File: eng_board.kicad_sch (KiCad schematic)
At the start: 54 parts, among them J1 Conn_01x12, J2 Conn_01x12, U1 LT3420, U12 TLV74318, U19 XS-LCC-01, U2 ADS7047, U5 ADS7047, U6 ADS7047, U7 TLV74325

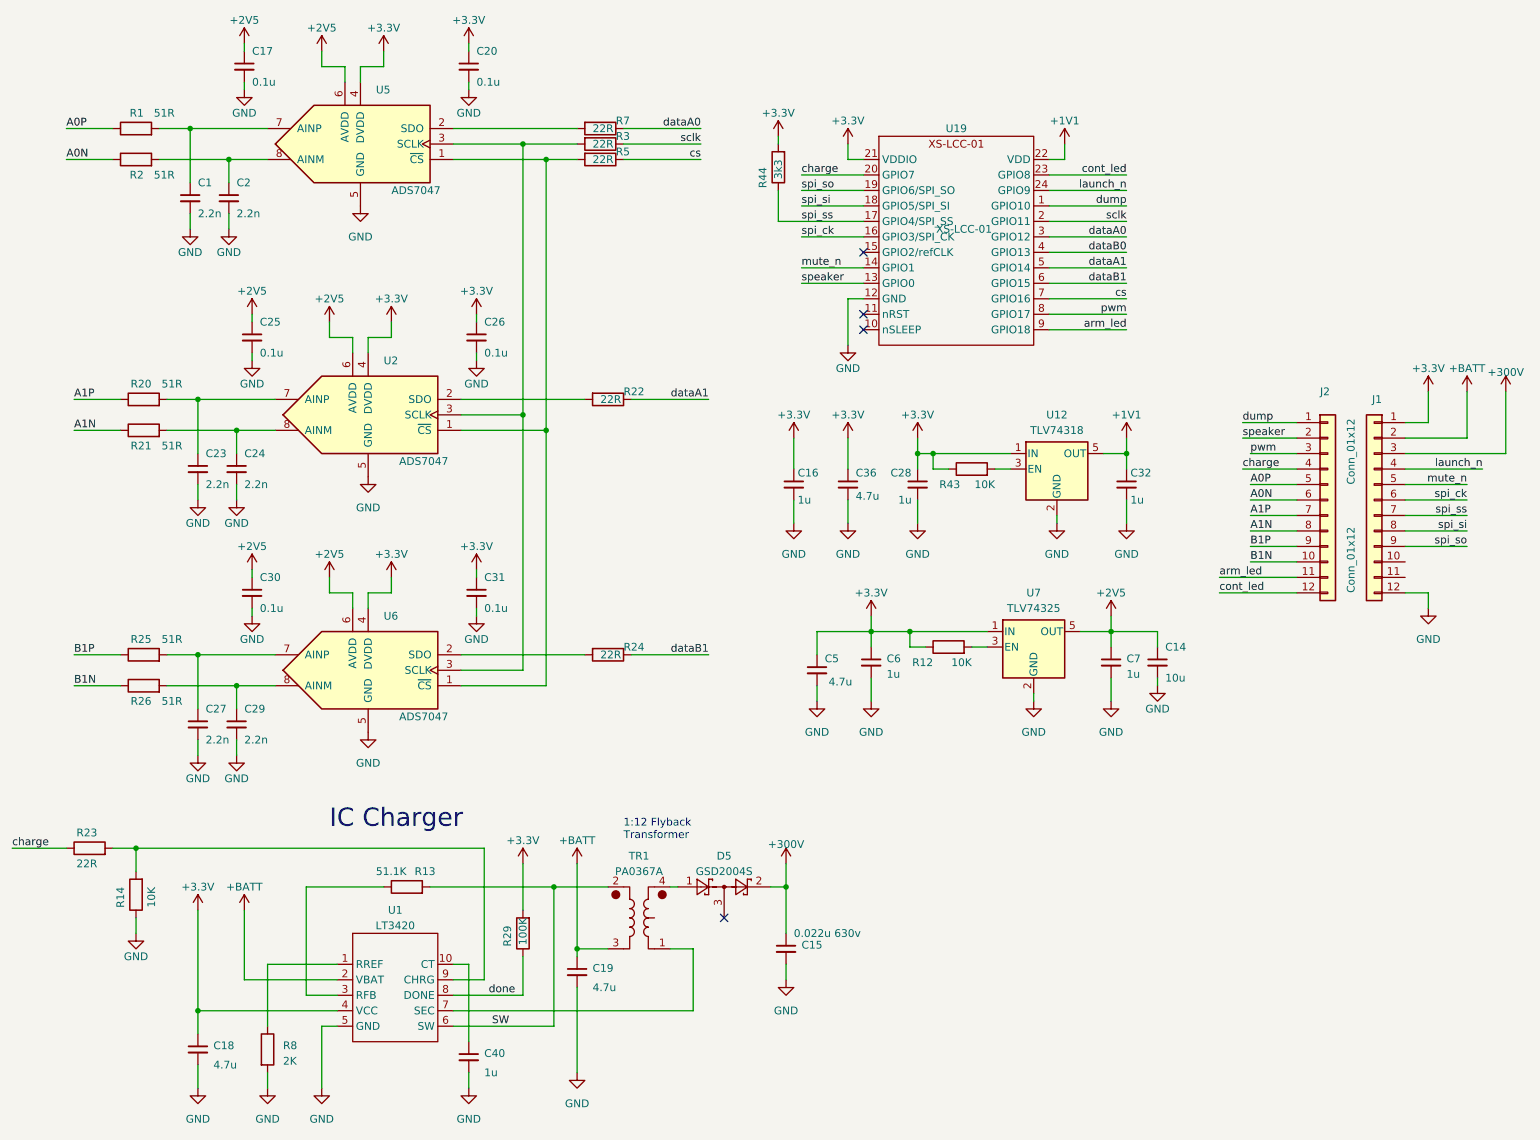
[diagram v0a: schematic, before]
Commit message: change back to dual ADCs (with internal refs) for now. Leave the low cost ADCs to the future
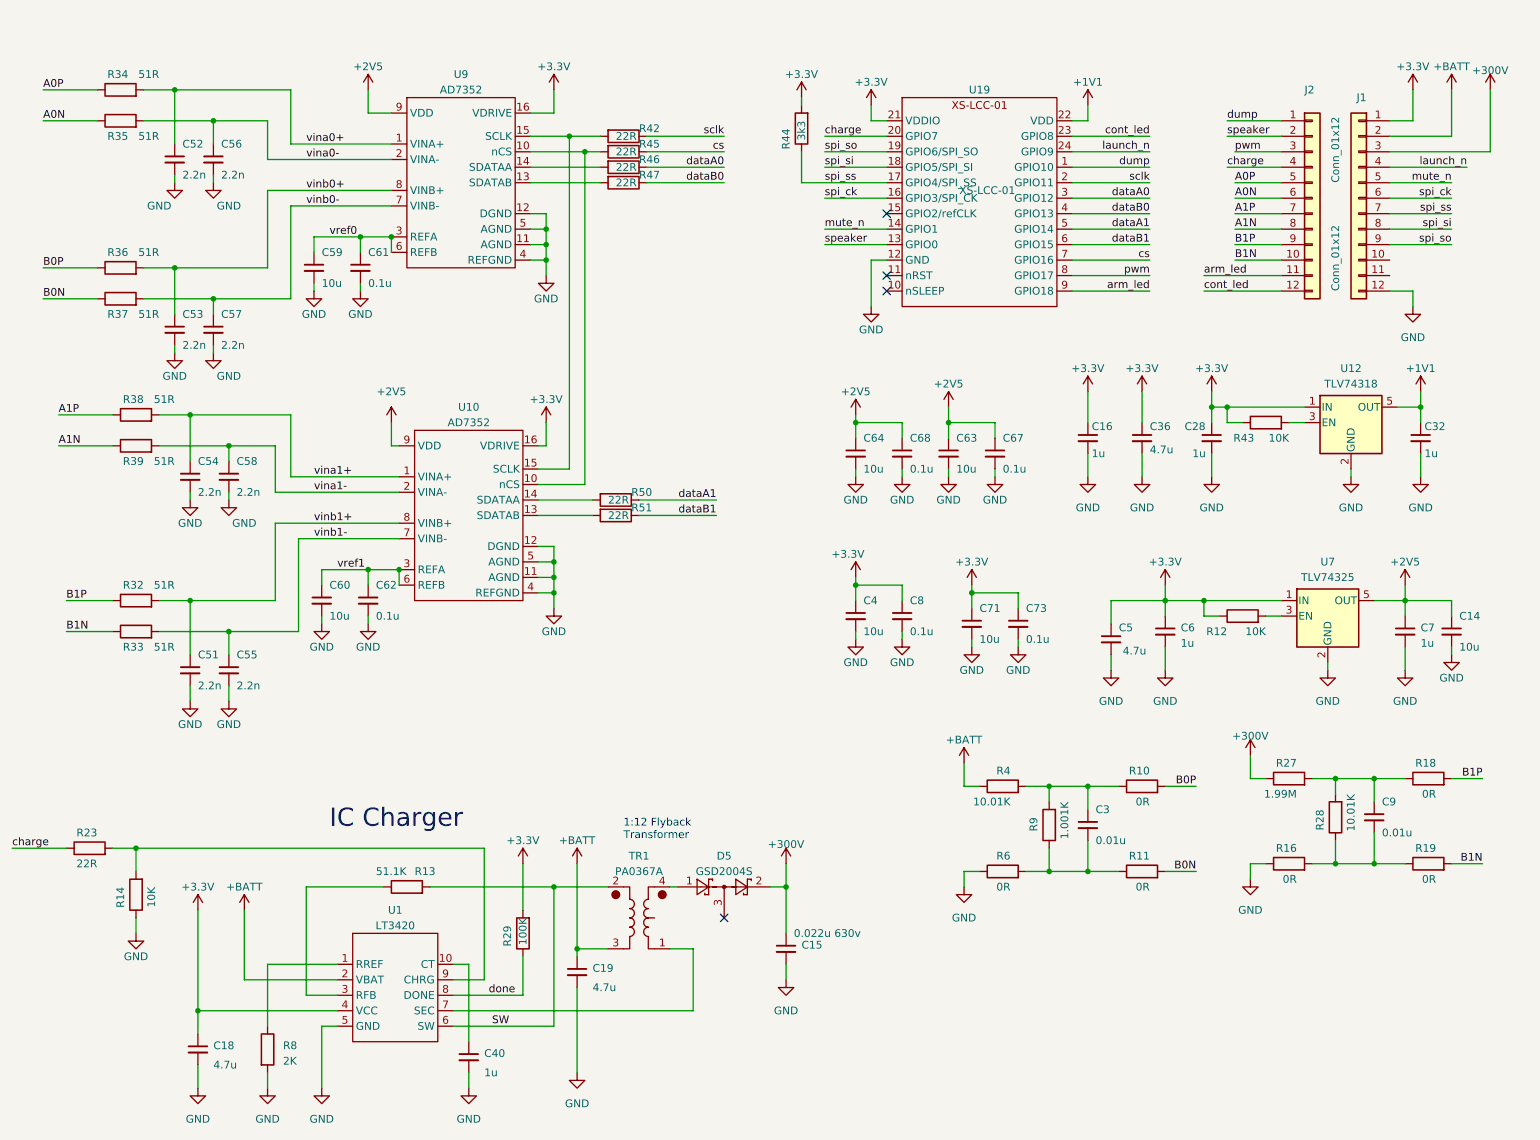
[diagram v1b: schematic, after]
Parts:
- removed C1, C2, C23, C24, C27, C29: 2.2n, Capacitor_SMD:C_0603_1608Metric, symbol Device:C_Small
- removed C17, C20, C25, C26, C30, C31: 0.1u, Capacitor_SMD:C_0603_1608Metric, symbol Device:C_Small
- removed R1, R2, R20, R21, R25, R26: 51R, Resistor_SMD:R_0603_1608Metric, symbol Device:R
- removed R22, R24, R3, R5, R7: 22R, Resistor_SMD:R_0603_1608Metric, symbol Device:R
- removed U2, U5, U6: ADS7047, Package_DFN_QFN:VDFN-8-1EP_2x2mm_P0.5mm_EP0.9x1.7mm, symbol myspace:ADS7047
- added C3, C9: 0.01u, Capacitor_SMD:C_0603_1608Metric, symbol Device:C_Small
- added C4, C59, C60, C63, C64, C71: 10u, Capacitor_SMD:C_1206_3216Metric, symbol Device:C_Small
- added C51, C52, C53, C54, C55, C56, C57, C58: 2.2n, Capacitor_SMD:C_0603_1608Metric, symbol Device:C_Small
- added C61, C62, C67, C68, C73, C8: 0.1u, Capacitor_SMD:C_0603_1608Metric, symbol Device:C_Small
- added R10, R11, R16, R18, R19, R6: 0R, Resistor_SMD:R_0603_1608Metric, symbol Device:R
- added R27: 1.99M, Resistor_SMD:R_0603_1608Metric, symbol Device:R
- added R28, R4: 10.01K, Resistor_SMD:R_0603_1608Metric, symbol Device:R
- added R32, R33, R34, R35, R36, R37, R38, R39: 51R, Resistor_SMD:R_0603_1608Metric, symbol Device:R
- added R42, R45, R46, R47, R50, R51: 22R, Resistor_SMD:R_0603_1608Metric, symbol Device:R
- added R9: 1.001K, Resistor_SMD:R_0603_1608Metric, symbol Device:R
- added U10, U9: AD7352, Package_SO:TSSOP-16_4.4x5mm_P0.65mm, symbol myspace:AD7352
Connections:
- net +2V5: now also C63.1, C64.1, C67.1, C68.1, U10.9 (VDD), U9.9 (VDD)
- net +3.3V: now also C4.1, C71.1, C73.1, C8.1, U10.16 (VDRIVE), U9.16 (VDRIVE)
- net +300V: now also R27.1
- net +BATT: now also R4.1
- net A0N: now also R35.1
- net A0P: now also R34.1
- net A1N: now also R39.1
- net A1P: now also R38.1
- net B1N: now also R19.2, R33.1
- net B1P: now also R18.2, R32.1
- net GND: now also C4.2, C51.2, C52.2, C53.2, C54.2, C55.2, C56.2, C57.2, C58.2, C59.2, C60.2, C61.2, C62.2, C63.2, C64.2, C67.2, C68.2, C71.2, C73.2, C8.2, R16.1, R6.1, U10.11 (AGND), U10.12 (DGND), U10.4 (REFGND), U10.5 (AGND), U9.11 (AGND), U9.12 (DGND), U9.4 (REFGND), U9.5 (AGND)
- net cs: now also R45.1
- net dataA0: now also R46.1
- net dataA1: now also R50.1
- net dataB0: now also R47.1
- net dataB1: now also R51.1
- net sclk: now also R42.1
- new net: R47.2, U9.13 (SDATAB)
- new net: R45.2, U10.10 (nCS), U9.10 (nCS)
- new net: C3.2, R11.1, R6.2, R9.1
- new net: C3.1, R10.1, R4.2, R9.2
- new net: R51.2, U10.13 (SDATAB)
- new net: R50.2, U10.14 (SDATAA)
- new net: R42.2, U10.15 (SCLK), U9.15 (SCLK)
- new net: C9.2, R16.2, R19.1, R28.1
- new net: R46.2, U9.14 (SDATAA)
- new net: C9.1, R18.1, R27.2, R28.2
- new net B0N: R11.2, R37.1
- new net B0P: R10.2, R36.1
- new net vina0+: C52.1, R34.2, U9.1 (VINA+)
- new net vina0-: C56.1, R35.2, U9.2 (VINA-)
- new net vina1+: C54.1, R38.2, U10.1 (VINA+)
- new net vina1-: C58.1, R39.2, U10.2 (VINA-)
- new net vinb0+: C53.1, R36.2, U9.8 (VINB+)
- new net vinb0-: C57.1, R37.2, U9.7 (VINB-)
- new net vinb1+: C51.1, R32.2, U10.8 (VINB+)
- new net vinb1-: C55.1, R33.2, U10.7 (VINB-)
- new net vref0: C59.1, C61.1, U9.3 (REFA), U9.6 (REFB)
- new net vref1: C60.1, C62.1, U10.3 (REFA), U10.6 (REFB)
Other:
- moved on the sheet: C14, C16, C28, C32, C36, C5, C6, C7, J1, J2, R12, R43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
